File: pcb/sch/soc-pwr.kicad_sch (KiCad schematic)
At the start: 23 parts, among them U1 XC7Z020CLG484

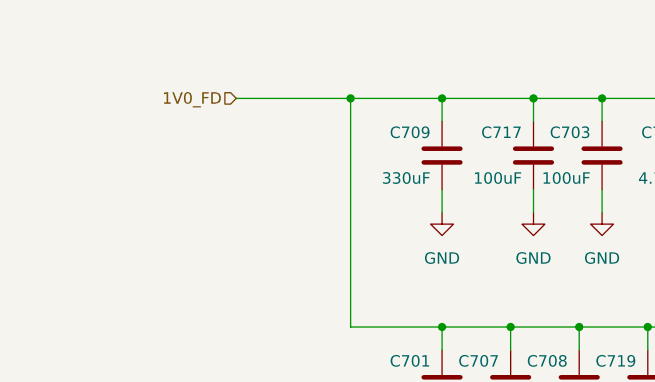
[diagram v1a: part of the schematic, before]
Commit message: byte swapping and rough layout
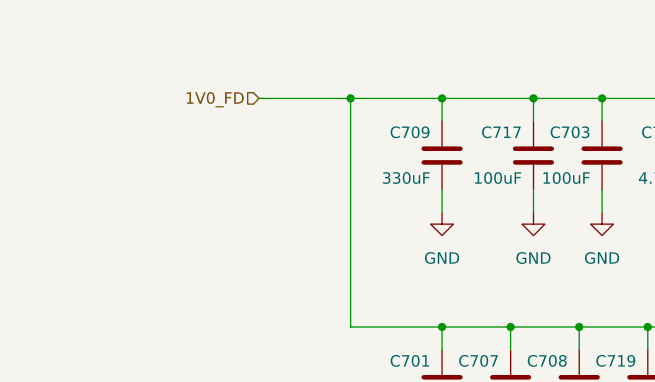
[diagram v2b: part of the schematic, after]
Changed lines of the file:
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@@
 	)
 	(junction
+		(at 53.34 27.94)
+		(diameter 0)
+		(color 0 0 0 0)
+	)
+	(junction
 		(at 251.46 71.12)
 		(diameter 0)
@@
 	)
 	(junction
-		(at 53.34 27.94)
-		(diameter 0)
-		(color 0 0 0 0)
-	)
-	(junction
 		(at 193.04 27.94)
 		(diameter 0)
@@
 	(wire
 		(pts
-			(xy 40.64 27.94) (xy 53.34 27.94)
+			(xy 43.18 27.94) (xy 53.34 27.94)
 		)
 		(stroke
@@
 	(hierarchical_label "1V0_FD"
 		(shape input)
-		(at 40.64 27.94 180)
+		(at 43.18 27.94 180)
 		(effects
 			(font

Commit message: power
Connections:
- net 1V0_FD renamed 1V0_Z
- net 1V8_FD renamed 1V8_Z
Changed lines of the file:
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@@
 		)
 	)
-	(hierarchical_label "1V0_FD"
+	(hierarchical_label "1V0_Z"
 		(shape input)
 		(at 43.18 27.94 180)
@@
 		)
 	)
-	(hierarchical_label "1V8_FD"
+	(hierarchical_label "1V8_Z"
 		(shape input)
 		(at 248.92 27.94 0)
